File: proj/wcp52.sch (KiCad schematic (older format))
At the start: 19 parts, among them J2 IN1, J3 IN2, J4 OUT, J5 CONN-PJ-037A, J7 AUX

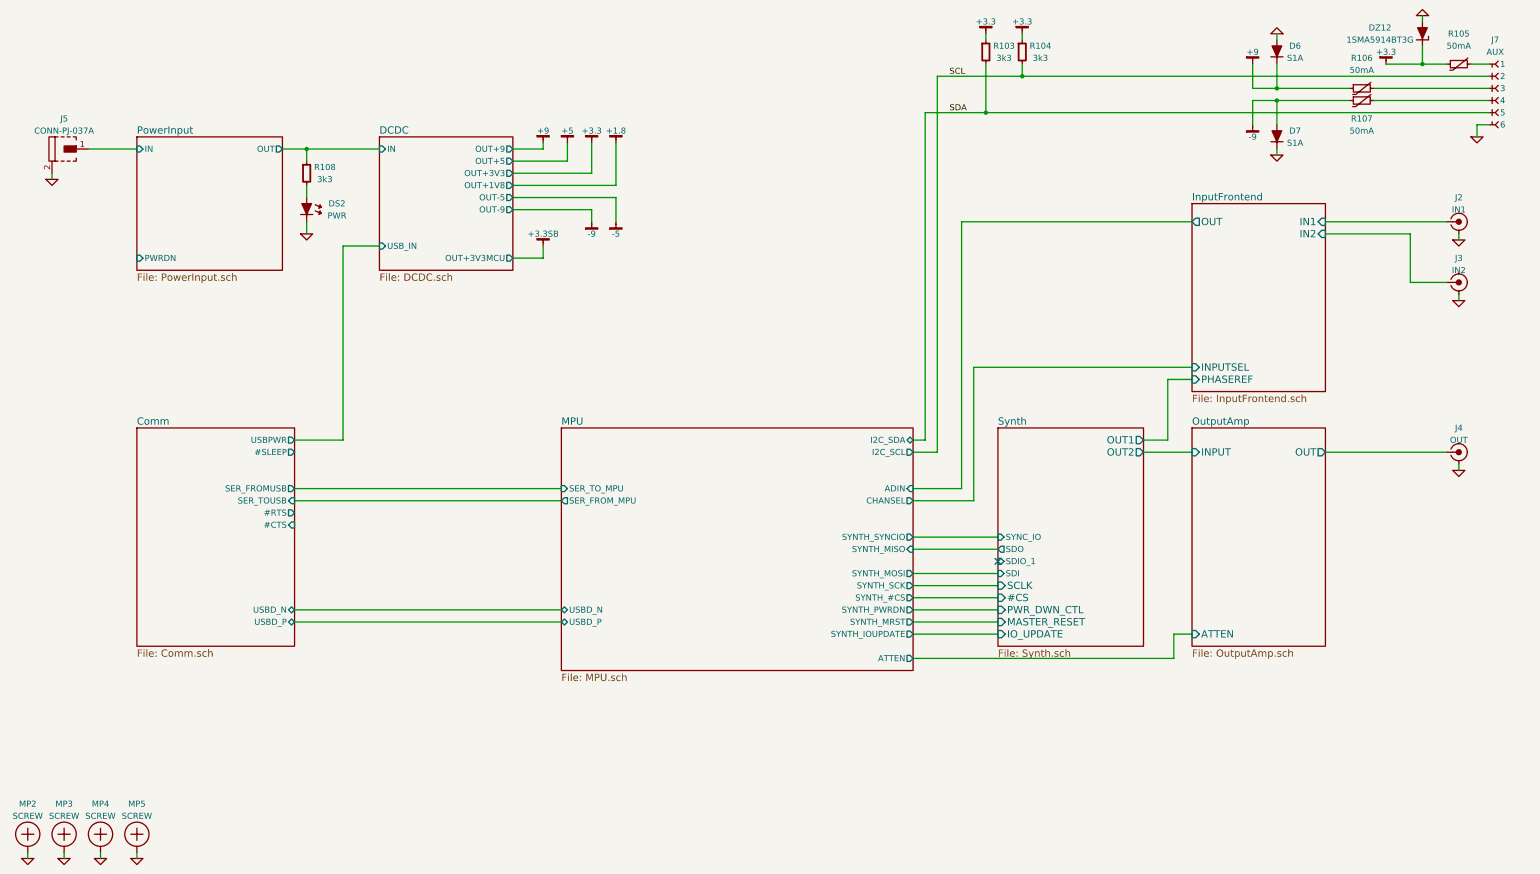
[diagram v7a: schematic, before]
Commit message: Clean up resistor BOM
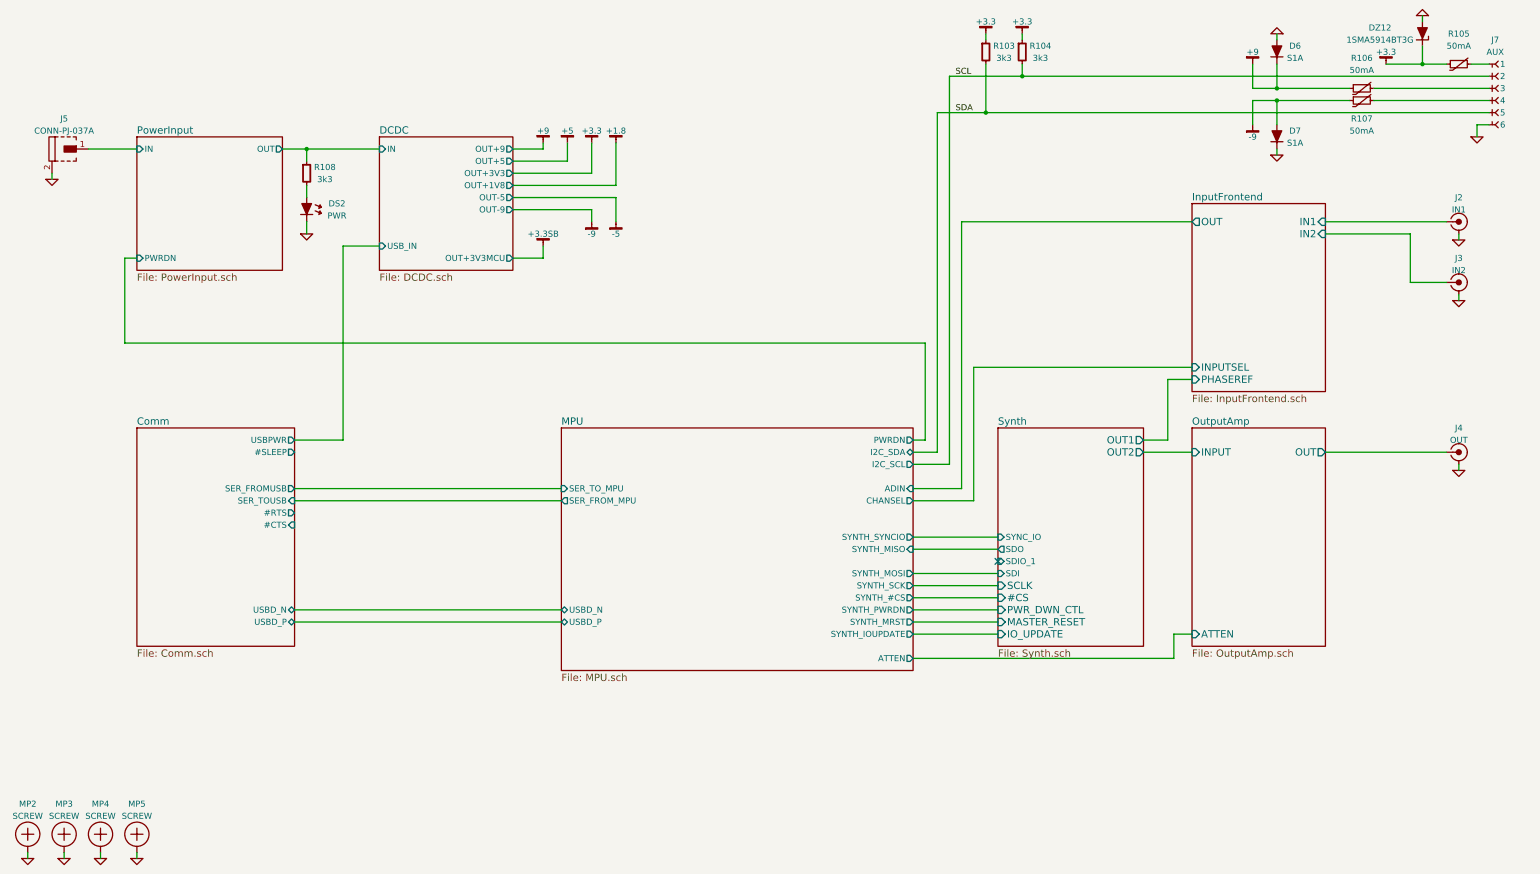
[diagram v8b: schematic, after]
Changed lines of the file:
@@
 	1    0    0    -1
 $EndComp
-Text Label 8600 1100 0    50   ~ 0
+Text Label 8650 1100 0    50   ~ 0
 SCL
-Text Label 8600 1400 0    50   ~ 0
+Text Label 8650 1400 0    50   ~ 0
 SDA
 $Comp
@@
 F14 "SYNTH_MOSI" O R 8300 5200 50
 F15 "ADIN" I R 8300 4500 50
-F16 "I2C_SDA" B R 8300 4100 50
-F17 "I2C_SCL" O R 8300 4200 50
+F16 "I2C_SDA" B R 8300 4200 50
+F17 "I2C_SCL" O R 8300 4300 50
 F18 "ATTEN" O R 8300 5900 50
+F19 "PWRDN" O R 8300 4100 50
 $EndSheet
 $Comp
@@
 	13050 1500 12950 1500
 Wire Wire Line
-	8500 1100 13050 1100
-Wire Wire Line
-	8400 1400 13050 1400
+	8600 1100 13050 1100
+Wire Wire Line
+	8500 1400 13050 1400
 Wire Wire Line
 	11100 1200 11100 1000
@@
 Connection ~ 8900 1400
 Wire Wire Line
-	8300 4100 8400 4100
-Wire Wire Line
-	8400 4100 8400 1400
-Wire Wire Line
 	8300 4200 8500 4200
 Wire Wire Line
-	8500 4200 8500 1100
+	8500 4200 8500 1400
+Wire Wire Line
+	8300 4300 8600 4300
+Wire Wire Line
+	8600 4300 8600 1100
 $Comp
 L THERM R107
@@
 Wire Wire Line
 	3300 2400 3300 2300
+Wire Wire Line
+	8300 4100 8400 4100
+Wire Wire Line
+	8400 4100 8400 3300
+Wire Wire Line
+	8400 3300 1800 3300
+Wire Wire Line
+	1800 3300 1800 2600
+Wire Wire Line
+	1800 2600 1900 2600
 $EndSCHEMATC
